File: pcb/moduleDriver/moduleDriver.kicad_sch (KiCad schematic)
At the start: 44 parts, among them J1 MOTOR, J10 Sensor, J11 Power, J12 Power, J13 Power, J14 LOOPBACK, J2 MOTOR, J3 MOTOR, J4 MOTOR, J5 IDC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

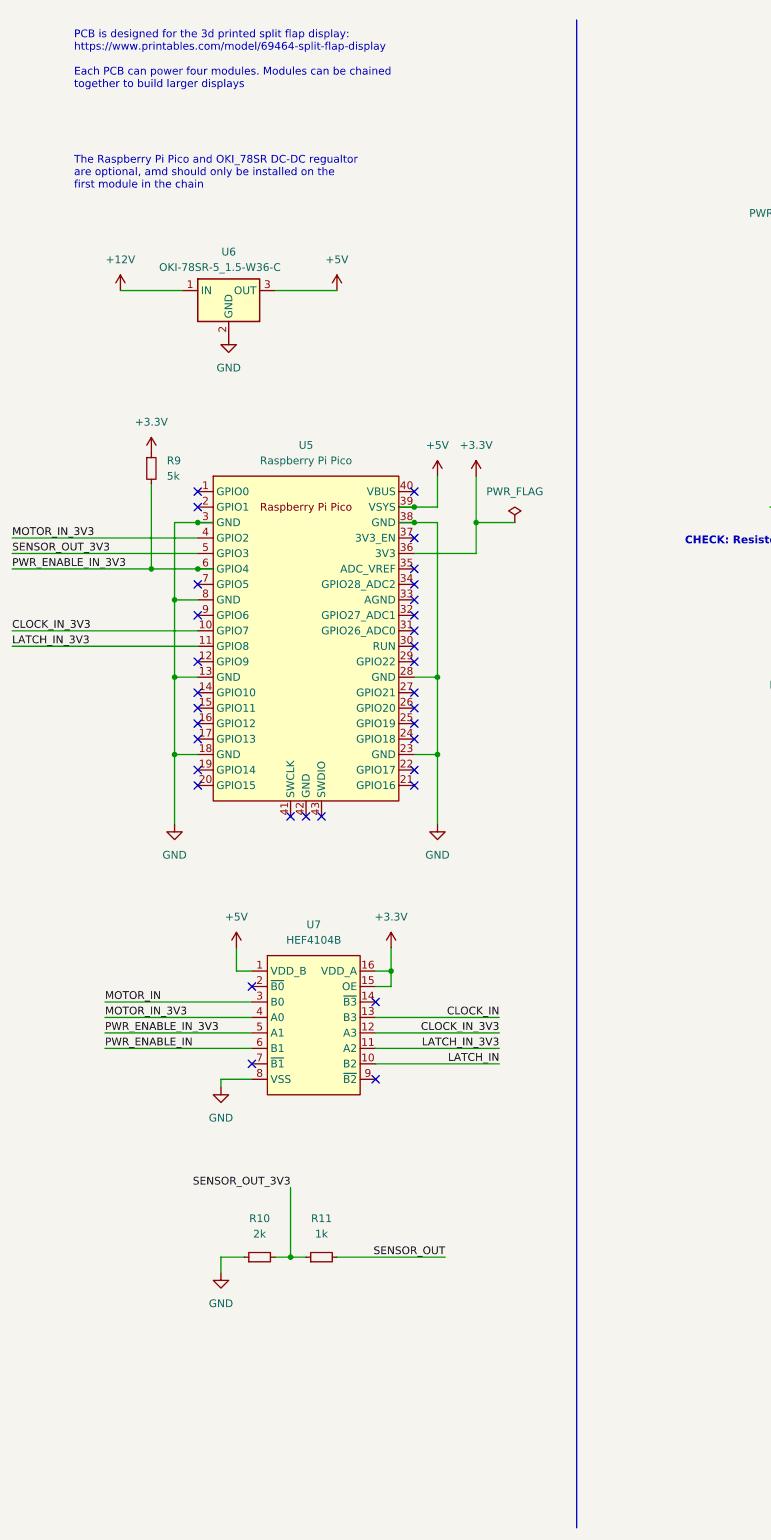
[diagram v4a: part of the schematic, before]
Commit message: Inital layout for voltage level translation
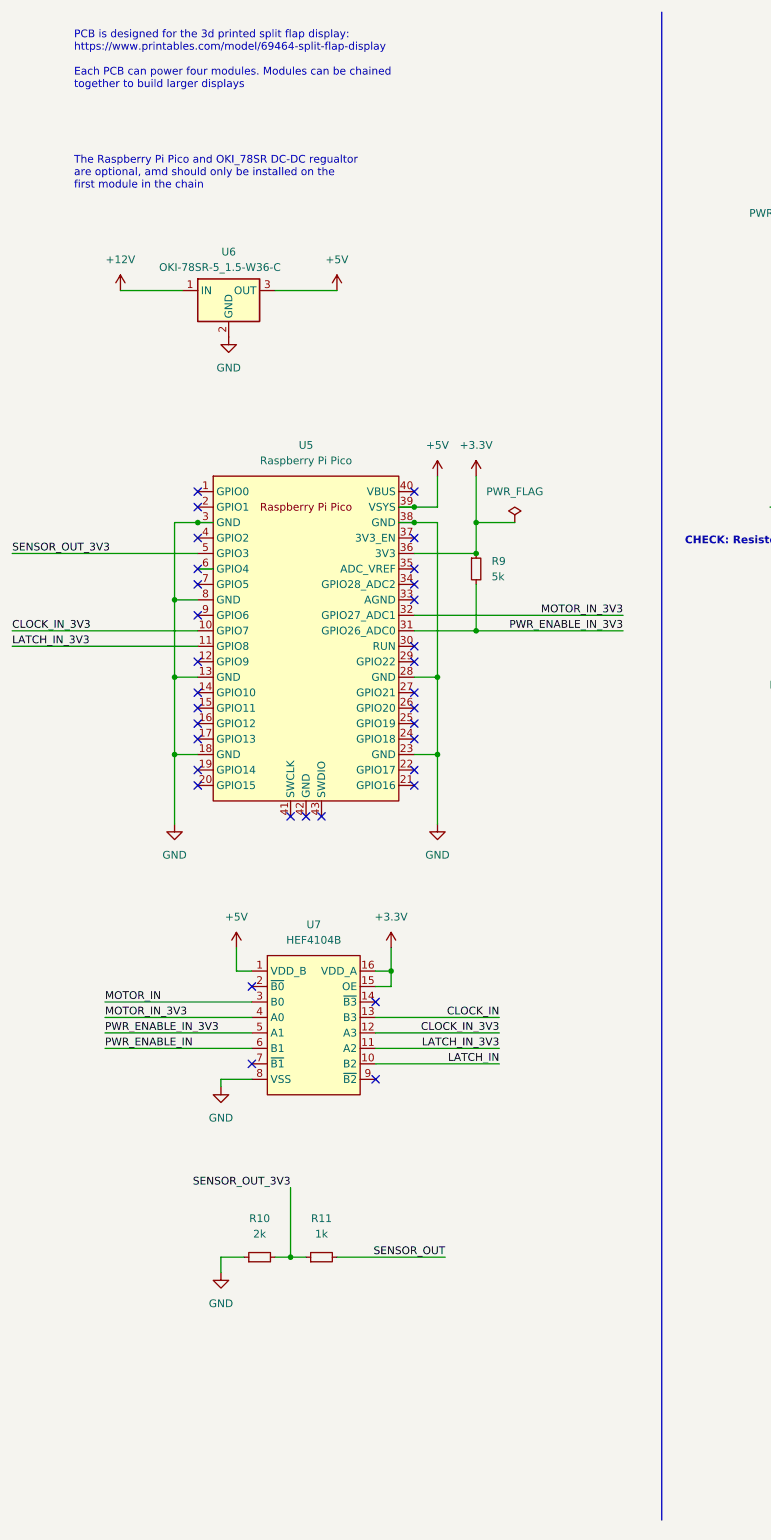
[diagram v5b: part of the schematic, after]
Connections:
- net MOTOR_IN_3V3: now also U5.32 (GPIO27_ADC1); no longer U5.4 (GPIO2)
- net PWR_ENABLE_IN_3V3: now also U5.31 (GPIO26_ADC0); no longer U5.6 (GPIO4)
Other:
- moved on the sheet: R9
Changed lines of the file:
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@@
   (junction (at 226.06 252.73) (diameter 0) (color 0 0 0 0)
   )
+  (junction (at 91.44 123.19) (diameter 0) (color 0 0 0 0)
+  )
   (junction (at 212.09 59.69) (diameter 0) (color 0 0 0 0)
   )
-  (junction (at 45.72 113.03) (diameter 0) (color 0 0 0 0)
-  )
   (junction (at 309.88 91.44) (diameter 0) (color 0 0 0 0)
   )
@@
   (junction (at 60.96 226.06) (diameter 0) (color 0 0 0 0)
   )
-  (junction (at 38.1 113.03) (diameter 0) (color 0 0 0 0)
-  )
   (junction (at 372.11 48.26) (diameter 0) (color 0 0 0 0)
   )
@@
   )
   (junction (at 156.21 38.1) (diameter 0) (color 0 0 0 0)
+  )
+  (junction (at 91.44 110.49) (diameter 0) (color 0 0 0 0)
   )
   (junction (at 177.8 250.19) (diameter 0) (color 0 0 0 0)
@@
   (no_connect (at 66.04 153.67))
   (no_connect (at 297.18 66.04))
+  (no_connect (at 45.72 113.03))
   (no_connect (at 81.28 100.33))
   (no_connect (at 297.18 71.12))
@@
   (no_connect (at 60.96 153.67))
   (no_connect (at 81.28 140.97))
+  (no_connect (at 45.72 107.95))
   (no_connect (at 297.18 63.5))
-  (no_connect (at 81.28 120.65))
   (no_connect (at 45.72 115.57))
   (no_connect (at 45.72 140.97))
@@
   (no_connect (at 81.28 135.89))
   (no_connect (at 81.28 148.59))
-  (no_connect (at 81.28 123.19))
   (no_connect (at 81.28 125.73))
   (wire (pts (xy 281.94 50.8) (xy 297.18 50.8))
@@
     (stroke (width 0) (type default) (color 0 0 0 0))
   )
-  (wire (pts (xy 15.24 107.95) (xy 45.72 107.95))
+  (wire (pts (xy 81.28 120.65) (xy 115.57 120.65))
     (stroke (width 0) (type default) (color 0 0 0 0))
   )
@@
     (stroke (width 0) (type default) (color 0 0 0 0))
   )
-  (polyline (pts (xy 107.95 22.86) (xy 107.95 270.51))
+  (polyline (pts (xy 121.92 21.59) (xy 121.92 269.24))
     (stroke (width 0) (type default) (color 0 0 0 0))
   )
@@
     (stroke (width 0) (type default) (color 0 0 0 0))
   )
-  (wire (pts (xy 15.24 113.03) (xy 38.1 113.03))
+  (wire (pts (xy 81.28 123.19) (xy 91.44 123.19))
     (stroke (width 0) (type default) (color 0 0 0 0))
   )
@@
     (stroke (width 0) (type default) (color 0 0 0 0))
   )
+  (wire (pts (xy 91.44 123.19) (xy 115.57 123.19))
+    (stroke (width 0) (type default) (color 0 0 0 0))
+  )
   (wire (pts (xy 147.32 190.5) (xy 170.18 190.5))
     (stroke (width 0) (type default) (color 0 0 0 0))
@@
     (stroke (width 0) (type default) (color 0 0 0 0))
   )
-  (wire (pts (xy 38.1 99.06) (xy 38.1 113.03))
-    (stroke (width 0) (type default) (color 0 0 0 0))
-  )
   (wire (pts (xy 250.19 182.88) (xy 250.19 198.12))
     (stroke (width 0) (type default) (color 0 0 0 0))
@@
     (stroke (width 0) (type default) (color 0 0 0 0))
   )
-  (wire (pts (xy 38.1 113.03) (xy 45.72 113.03))
-    (stroke (width 0) (type default) (color 0 0 0 0))
-  )
   (wire (pts (xy 276.86 193.04) (xy 299.72 193.04))
     (stroke (width 0) (type default) (color 0 0 0 0))
@@
   )
   (wire (pts (xy 194.31 198.12) (xy 217.17 198.12))
+    (stroke (width 0) (type default) (color 0 0 0 0))
+  )
+  (wire (pts (xy 91.44 115.57) (xy 91.44 123.19))
     (stroke (width 0) (type default) (color 0 0 0 0))
   )
@@
     (effects (font (size 1.27 1.27)) (justify right bottom))
   )
-  (label "MOTOR_IN_3V3" (at 15.24 107.95 0)
-    (effects (font (size 1.27 1.27)) (justify left bottom))
+  (label "MOTOR_IN_3V3" (at 115.57 120.65 180)
+    (effects (font (size 1.27 1.27)) (justify right bottom))
   )
   (label "MOTOR_C_PHASE_A" (at 229.87 187.96 0)
     (effects (font (size 1.27 1.27)) (justify left bottom))
   )
-  (label "PWR_ENABLE_IN_3V3" (at 15.24 113.03 0)
-    (effects (font (size 1.27 1.27)) (justify left bottom))
+  (label "PWR_ENABLE_IN_3V3" (at 115.57 123.19 180)
+    (effects (font (size 1.27 1.27)) (justify right bottom))
   )
   (label "CLOCK_IN" (at 95.25 186.69 180)
@@
     (pin "5")
   )
-  (symbol (lib_id "Device:R_Small") (at 38.1 96.52 0) (unit 1)
-    (in_bom yes) (on_board yes) (fields_autoplaced)
-    (property "Reference" "R9" (id 0) (at 40.64 95.2499 0)
-      (effects (font (size 1.27 1.27)) (justify left))
-    )
-    (property "Value" "5k" (id 1) (at 40.64 97.7899 0)
-      (effects (font (size 1.27 1.27)) (justify left))
-    )
-    (property "Footprint" "Resistor_SMD:R_0603_1608Metric" (id 2) (at 38.1 96.52 0)
-      (effects (font (size 1.27 1.27)) hide)
-    )
-    (property "Datasheet" "~" (id 3) (at 38.1 96.52 0)
+  (symbol (lib_id "Device:R_Small") (at 91.44 113.03 0) (unit 1)
+    (in_bom yes) (on_board yes) (fields_autoplaced)
+    (property "Reference" "R9" (id 0) (at 93.98 111.7599 0)
+      (effects (font (size 1.27 1.27)) (justify left))
+    )
+    (property "Value" "5k" (id 1) (at 93.98 114.2999 0)
+      (effects (font (size 1.27 1.27)) (justify left))
+    )
+    (property "Footprint" "Resistor_SMD:R_0603_1608Metric" (id 2) (at 91.44 113.03 0)
+      (effects (font (size 1.27 1.27)) hide)
+    )
+    (property "Datasheet" "~" (id 3) (at 91.44 113.03 0)
       (effects (font (size 1.27 1.27)) hide)
     )
@@
     (pin "9")
   )
-  (symbol (lib_id "power:+3.3V") (at 38.1 93.98 0) (unit 1)
-    (in_bom yes) (on_board yes) (fields_autoplaced)
-    (property "Reference" "#PWR08" (id 0) (at 38.1 97.79 0)
-      (effects (font (size 1.27 1.27)) hide)
-    )
-    (property "Value" "+3.3V" (id 1) (at 38.1 88.9 0))
-    (property "Footprint" "" (id 2) (at 38.1 93.98 0)
-      (effects (font (size 1.27 1.27)) hide)
-    )
-    (property "Datasheet" "" (id 3) (at 38.1 93.98 0)
-      (effects (font (size 1.27 1.27)) hide)
-    )
-    (pin "1")
-  )
   (symbol (lib_id "power:+5V") (at 158.75 237.49 0) (unit 1)
     (in_bom yes) (on_board yes) (fields_autoplaced)
@@
       (reference "#PWR07") (unit 1) (value "GND") (footprint "")
     )
-    (path "/ccabcbe5-ca23-4cf7-a3c4-08d7d3171cac"
-      (reference "#PWR08") (unit 1) (value "+3.3V") (footprint "")
-    )
     (path "/7c798880-a3b2-48b5-bbd5-6f1056ffee83"
